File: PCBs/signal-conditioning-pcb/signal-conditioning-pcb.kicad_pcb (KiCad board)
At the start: 2 copper layers, 93 x 112 mm, 21 parts, among them J1 Conn_Coaxial, J2 Conn_Coaxial, J3 Conn_Coaxial, J5 Conn_01x04_Pin, M1 MountingHole_4.3mm_M4_ISO1458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, M2 MountingHole_4.3mm_M4_ISO1458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, M3 MountingHole_4.3mm_M4_ISO1458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, U1 LM358, U2 LM358

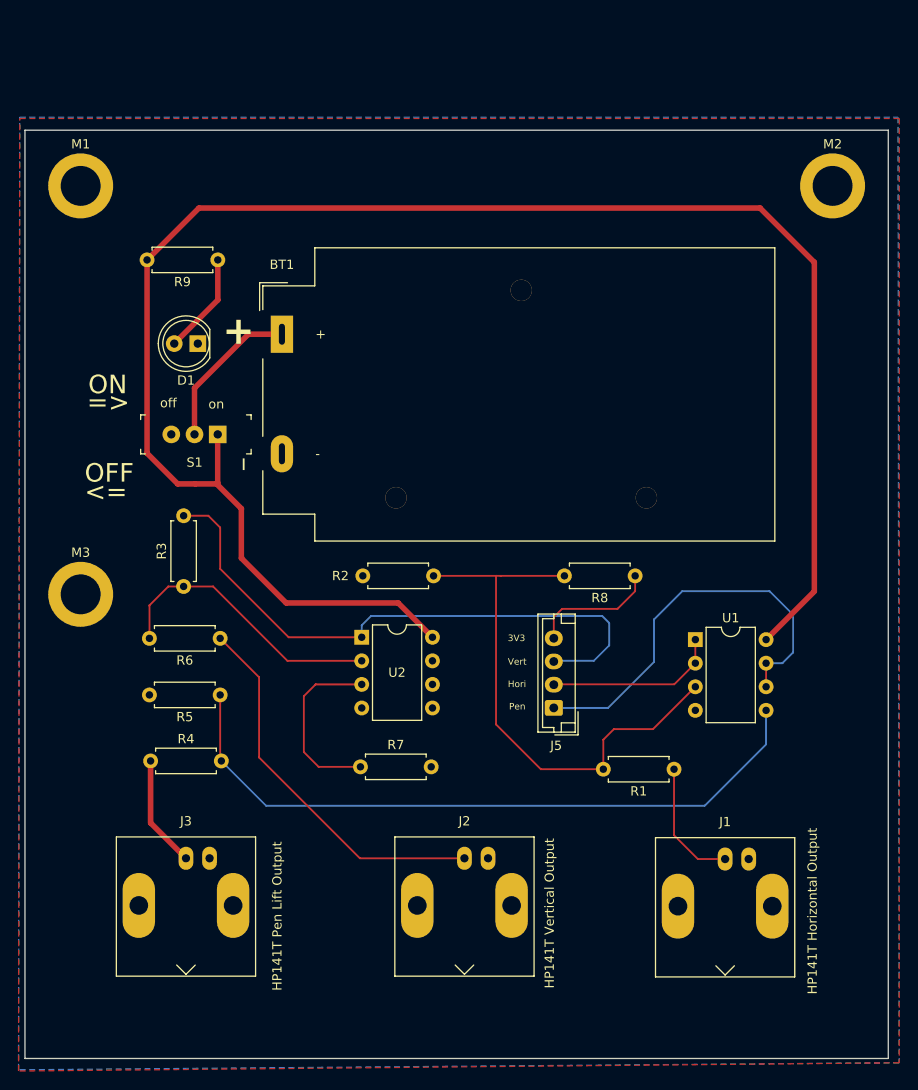
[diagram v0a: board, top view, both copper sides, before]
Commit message: Added GND mounting holes to SigConditioningCirc
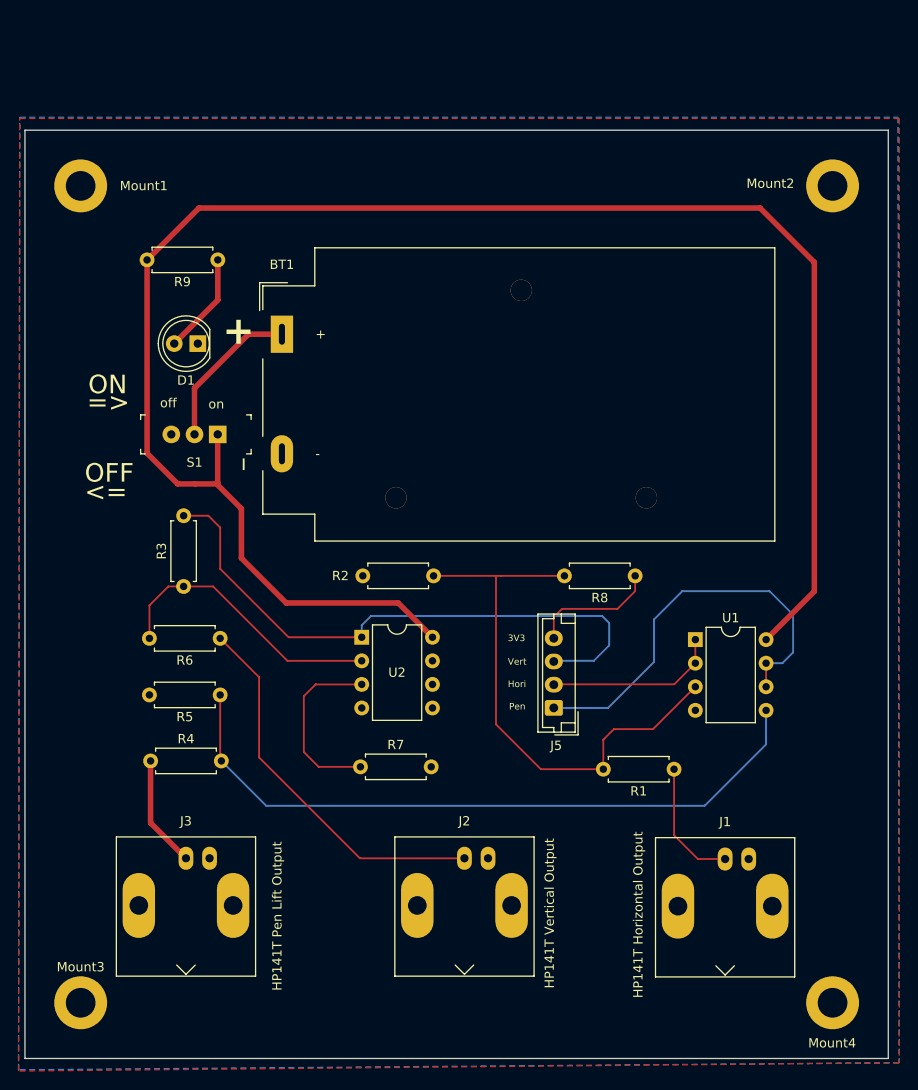
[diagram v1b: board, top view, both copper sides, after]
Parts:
- removed M1, M2, M3: MountingHole_4.3mm_M4_ISO14580_Pad, MountingHole:MountingHole_4.3mm_M4_ISO14580_Pad
- added Mount1: MountingHole_3.2mm_M3_ISO7380_Pad, MountingHole:MountingHole_3.2mm_M3_ISO7380_Pad, F.Cu at (99.4, 38.0)
- added Mount2: MountingHole_3.2mm_M3_ISO7380_Pad, MountingHole:MountingHole_3.2mm_M3_ISO7380_Pad, F.Cu at (180.4, 38.0)
- added Mount3: MountingHole_3.2mm_M3_ISO7380_Pad, MountingHole:MountingHole_3.2mm_M3_ISO7380_Pad, F.Cu at (99.4, 126.0)
- added Mount4: MountingHole_3.2mm_M3_ISO7380_Pad, MountingHole:MountingHole_3.2mm_M3_ISO7380_Pad, F.Cu at (180.4, 126.0)
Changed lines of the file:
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@@
   )
   (paper "A4")
+  (title_block
+    (title "HP141T Signal Conditioning Board")
+    (date "2025-04-04")
+    (rev "v01")
+    (company "University of  Cape Town")
+  )
   (layers
     (0 "F.Cu" signal)
@@
     )
   )
-  (footprint "MountingHole:MountingHole_4.3mm_M4_ISO14580_Pad" (layer "F.Cu")
-    (at 99.4 38)
-    (descr "Mounting Hole 4.3mm, M4, ISO14580")
-    (tags "mounting hole 4.3mm m4 iso14580")
-    (attr exclude_from_pos_files exclude_from_bom)
-    (fp_text reference "M1" (at 0 -4.5) (layer "F.SilkS")
-        (effects (font (size 1 1) (thickness 0.15)))
-    )
-    (fp_text value "MountingHole_4.3mm_M4_ISO14580_Pad" (at 19.599 -0.408 180) (layer "F.Fab")
-        (effects (font (size 1 1) (thickness 0.15)))
-    )
-    (fp_text user "${REFERENCE}" (at 0 0) (layer "F.Fab")
-        (effects (font (size 1 1) (thickness 0.15)))
-    )
-    (fp_circle (center 0 0) (end 3.5 0)
-      (stroke (width 0.15) (type solid)) (fill none) (layer "Cmts.User"))
-    (fp_circle (center 0 0) (end 3.75 0)
-      (stroke (width 0.05) (type solid)) (fill none) (layer "F.CrtYd"))
-    (pad "1" thru_hole circle (at 0 0) (size 7 7) (drill 4.3) (layers "*.Cu" "*.Mask")
-      (net 3 "GND"))
-  )
   (footprint "Connector_Coaxial:BNC_Amphenol_B6252HB-NPP3G-50_Horizontal" (layer "F.Cu")
     (at 110.744 110.434 180)
@@
         (effects (font (size 1 1) (thickness 0.15)))
     )
-    (fp_text value "Conn_Coaxial" (at 0 6) (layer "F.Fab")
+    (fp_text value "Conn_Coaxial" (at -0.256 -9.916) (layer "F.Fab")
         (effects (font (size 1 1) (thickness 0.15)))
     )
@@
       (rotate (xyz 0 0 0))
     )
-  )
-  (footprint "MountingHole:MountingHole_4.3mm_M4_ISO14580_Pad" (layer "F.Cu")
-    (at 180.4 38)
-    (descr "Mounting Hole 4.3mm, M4, ISO14580")
-    (tags "mounting hole 4.3mm m4 iso14580")
-    (attr exclude_from_pos_files exclude_from_bom)
-    (fp_text reference "M2" (at 0 -4.5) (layer "F.SilkS")
-        (effects (font (size 1 1) (thickness 0.15)))
-    )
-    (fp_text value "MountingHole_4.3mm_M4_ISO14580_Pad" (at -20.888 -0.789) (layer "F.Fab")
-        (effects (font (size 1 1) (thickness 0.15)))
-    )
-    (fp_text user "${REFERENCE}" (at 0 0) (layer "F.Fab")
-        (effects (font (size 1 1) (thickness 0.15)))
-    )
-    (fp_circle (center 0 0) (end 3.5 0)
-      (stroke (width 0.15) (type solid)) (fill none) (layer "Cmts.User"))
-    (fp_circle (center 0 0) (end 3.75 0)
-      (stroke (width 0.05) (type solid)) (fill none) (layer "F.CrtYd"))
-    (pad "1" thru_hole circle (at 0 0) (size 7 7) (drill 4.3) (layers "*.Cu" "*.Mask")
-      (net 3 "GND"))
   )
   (footprint "Package_DIP:DIP-8_W7.62mm" (layer "F.Cu")
@@
     )
   )
+  (footprint "MountingHole:MountingHole_3.2mm_M3_ISO7380_Pad" (layer "F.Cu")
+    (at 99.4 38)
+    (descr "Mounting Hole 3.2mm, M3, ISO7380")
+    (tags "mounting hole 3.2mm m3 iso7380")
+    (attr exclude_from_pos_files exclude_from_bom)
+    (fp_text reference "Mount1" (at 6.8 0) (layer "F.SilkS")
+        (effects (font (size 1 1) (thickness 0.15)))
+    )
+    (fp_text value "MountingHole_3.2mm_M3_ISO7380_Pad" (at -2.75 21.15 90) (layer "F.Fab")
+        (effects (font (size 1 1) (thickness 0.15)))
+    )
+    (fp_text user "${REFERENCE}" (at 0 0) (layer "F.Fab")
+        (effects (font (size 1 1) (thickness 0.15)))
+    )
+    (fp_circle (center 0 0) (end 2.85 0)
+      (stroke (width 0.15) (type solid)) (fill none) (layer "Cmts.User"))
+    (fp_circle (center 0 0) (end 3.1 0)
+      (stroke (width 0.05) (type solid)) (fill none) (layer "F.CrtYd"))
+    (pad "1" thru_hole circle (at 0 0) (size 5.7 5.7) (drill 3.2) (layers "*.Cu" "*.Mask")
+      (net 3 "GND"))
+  )
   (footprint "Resistor_THT:R_Axial_DIN0207_L6.3mm_D2.5mm_P7.62mm_Horizontal" (layer "F.Cu")
     (at 114.427 86.741 180)
@@
     )
   )
-  (footprint "MountingHole:MountingHole_4.3mm_M4_ISO14580_Pad" (layer "F.Cu")
-    (at 99.4 82)
-    (descr "Mounting Hole 4.3mm, M4, ISO14580")
-    (tags "mounting hole 4.3mm m4 iso14580")
+  (footprint "MountingHole:MountingHole_3.2mm_M3_ISO7380_Pad" (layer "F.Cu")
+    (at 99.4 126)
+    (descr "Mounting Hole 3.2mm, M3, ISO7380")
+    (tags "mounting hole 3.2mm m3 iso7380")
     (attr exclude_from_pos_files exclude_from_bom)
-    (fp_text reference "M3" (at 0 -4.5) (layer "F.SilkS")
-        (effects (font (size 1 1) (thickness 0.15)))
-    )
-    (fp_text value "MountingHole_4.3mm_M4_ISO14580_Pad" (at 0.168 21.632 90) (layer "F.Fab")
+    (fp_text reference "Mount3" (at 0 -3.85) (layer "F.SilkS")
+        (effects (font (size 1 1) (thickness 0.15)))
+    )
+    (fp_text value "MountingHole_3.2mm_M3_ISO7380_Pad" (at 0.1 -20.9 90) (layer "F.Fab")
         (effects (font (size 1 1) (thickness 0.15)))
     )
@@
         (effects (font (size 1 1) (thickness 0.15)))
     )
-    (fp_circle (center 0 0) (end 3.5 0)
+    (fp_circle (center 0 0) (end 2.85 0)
       (stroke (width 0.15) (type solid)) (fill none) (layer "Cmts.User"))
-    (fp_circle (center 0 0) (end 3.75 0)
+    (fp_circle (center 0 0) (end 3.1 0)
       (stroke (width 0.05) (type solid)) (fill none) (layer "F.CrtYd"))
-    (pad "1" thru_hole circle (at 0 0) (size 7 7) (drill 4.3) (layers "*.Cu" "*.Mask")
+    (pad "1" thru_hole circle (at 0 0) (size 5.7 5.7) (drill 3.2) (layers "*.Cu" "*.Mask")
       (net 3 "GND"))
   )
@@
       (net 19 "unconnected-(S1-Pad3)") (pintype "passive+no_connect"))
   )
+  (footprint "MountingHole:MountingHole_3.2mm_M3_ISO7380_Pad" (layer "F.Cu")
+    (at 180.4 38)
+    (descr "Mounting Hole 3.2mm, M3, ISO7380")
+    (tags "mounting hole 3.2mm m3 iso7380")
+    (attr exclude_from_pos_files exclude_from_bom)
+    (fp_text reference "Mount2" (at -6.7 -0.25) (layer "F.SilkS")
+        (effects (font (size 1 1) (thickness 0.15)))
+    )
+    (fp_text value "MountingHole_3.2mm_M3_ISO7380_Pad" (at 2.55 19.75 90) (layer "F.Fab")
+        (effects (font (size 1 1) (thickness 0.15)))
+    )
+    (fp_text user "${REFERENCE}" (at 0 0) (layer "F.Fab")
+        (effects (font (size 1 1) (thickness 0.15)))
+    )
+    (fp_circle (center 0 0) (end 2.85 0)
+      (stroke (width 0.15) (type solid)) (fill none) (layer "Cmts.User"))
+    (fp_circle (center 0 0) (end 3.1 0)
+      (stroke (width 0.05) (type solid)) (fill none) (layer "F.CrtYd"))
+    (pad "1" thru_hole circle (at 0 0) (size 5.7 5.7) (drill 3.2) (layers "*.Cu" "*.Mask")
+      (net 3 "GND"))
+  )
+  (footprint "MountingHole:MountingHole_3.2mm_M3_ISO7380_Pad" (layer "F.Cu")
+    (at 180.4 126)
+    (descr "Mounting Hole 3.2mm, M3, ISO7380")
+    (tags "mounting hole 3.2mm m3 iso7380")
+    (attr exclude_from_pos_files exclude_from_bom)
+    (fp_text reference "Mount4" (at -0.05 4.35) (layer "F.SilkS")
+        (effects (font (size 1 1) (thickness 0.15)))
+    )
+    (fp_text value "MountingHole_3.2mm_M3_ISO7380_Pad" (at 2.05 -19.8 90) (layer "F.Fab")
+        (effects (font (size 1 1) (thickness 0.15)))
+    )
+    (fp_text user "${REFERENCE}" (at 0 0) (layer "F.Fab")
+        (effects (font (size 1 1) (thickness 0.15)))
+    )
+    (fp_circle (center 0 0) (end 2.85 0)
+      (stroke (width 0.15) (type solid)) (fill none) (layer "Cmts.User"))
+    (fp_circle (center 0 0) (end 3.1 0)
+      (stroke (width 0.05) (type solid)) (fill none) (layer "F.CrtYd"))
+    (pad "1" thru_hole circle (at 0 0) (size 5.7 5.7) (drill 3.2) (layers "*.Cu" "*.Mask")
+      (net 3 "GND"))
+  )
   (footprint "Resistor_THT:R_Axial_DIN0207_L6.3mm_D2.5mm_P7.62mm_Horizontal" (layer "F.Cu")
     (at 114.173 45.974 180)
@@
     (effects (font (size 0.7 0.7) (thickness 0.1)) (justify left bottom))
   )
-  (gr_text "HP141T Horizontal Output" (at 178.816 125.095 90) (layer "F.SilkS")
+  (gr_text "HP141T Horizontal Output" (at 160.05 125.5 90) (layer "F.SilkS")
     (effects (font (size 1 1) (thickness 0.2)) (justify left bottom))
   )
